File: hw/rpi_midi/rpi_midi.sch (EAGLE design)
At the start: 47 parts, among them IC1 74HC14N, X1 WBTOR1, X2 WBTOR1, X3 WBTOR1, X4 WBTOR1

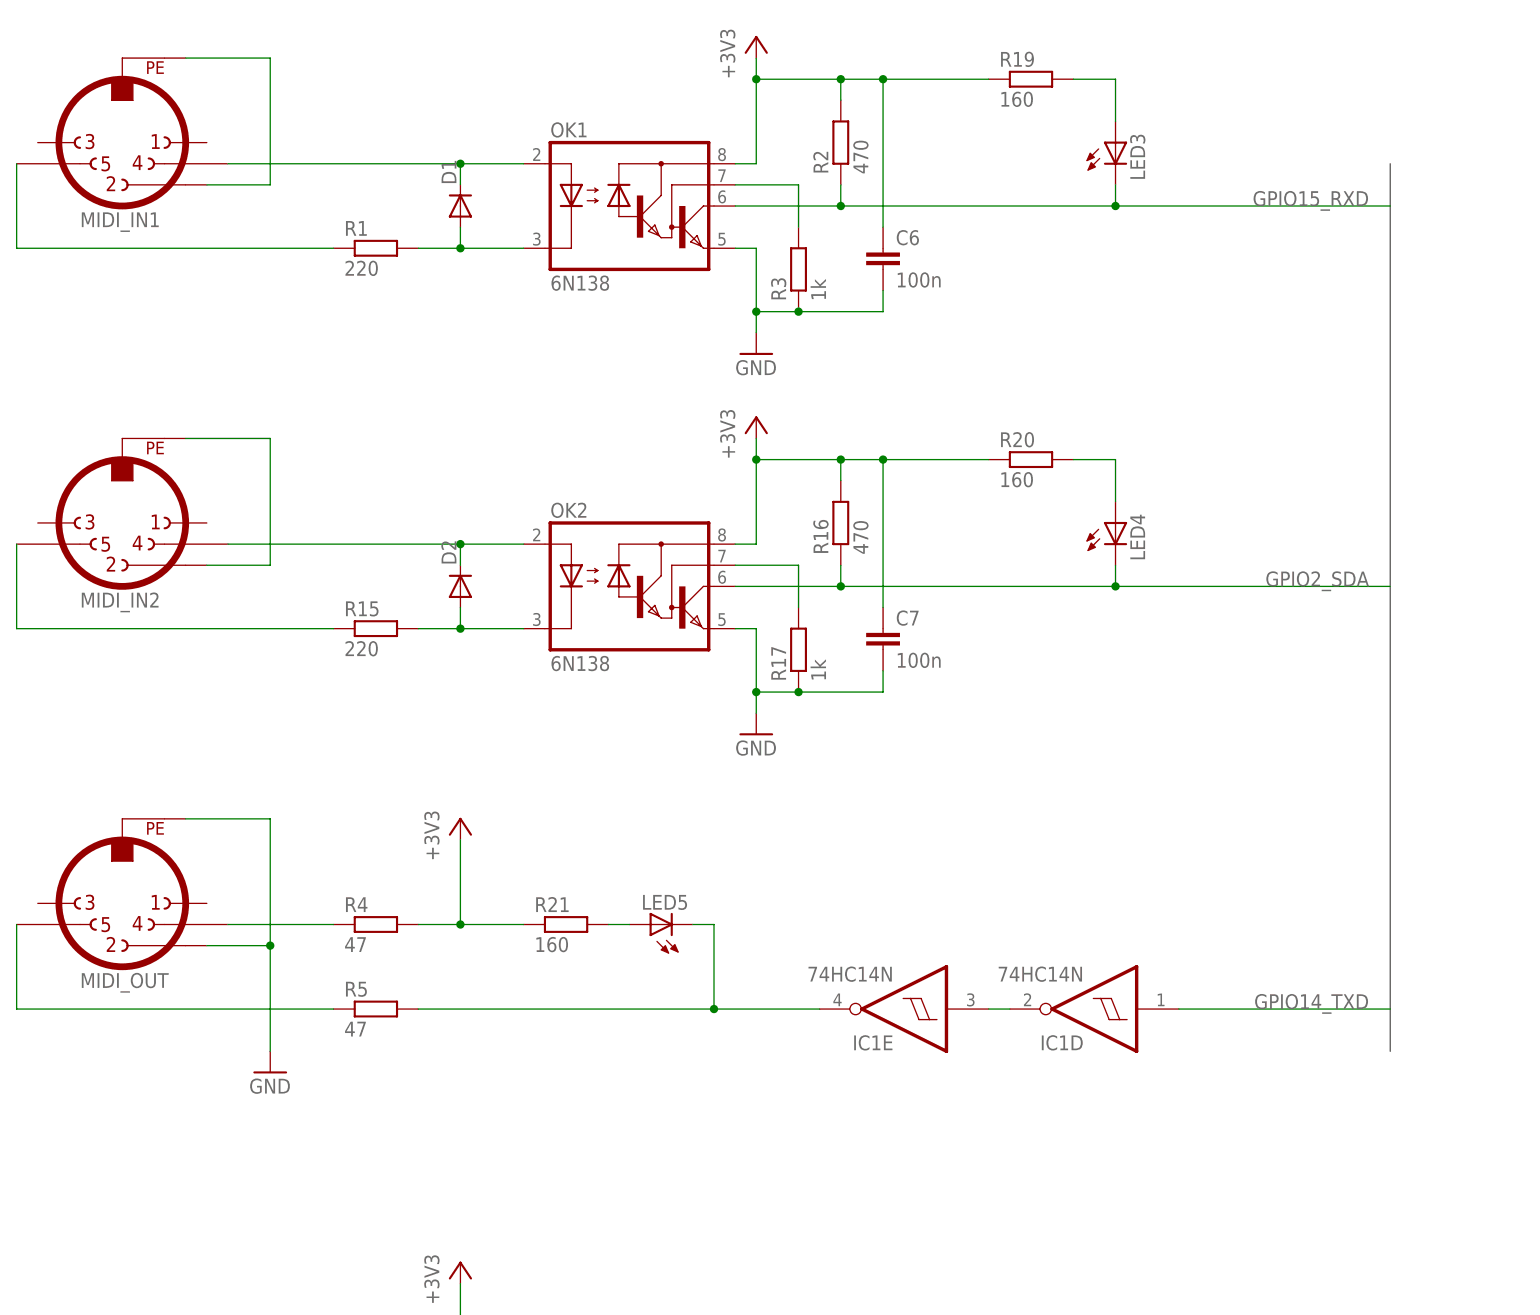
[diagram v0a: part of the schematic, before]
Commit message: The RPi MIDI extension board now features MIDI_OUT link detection capabilities
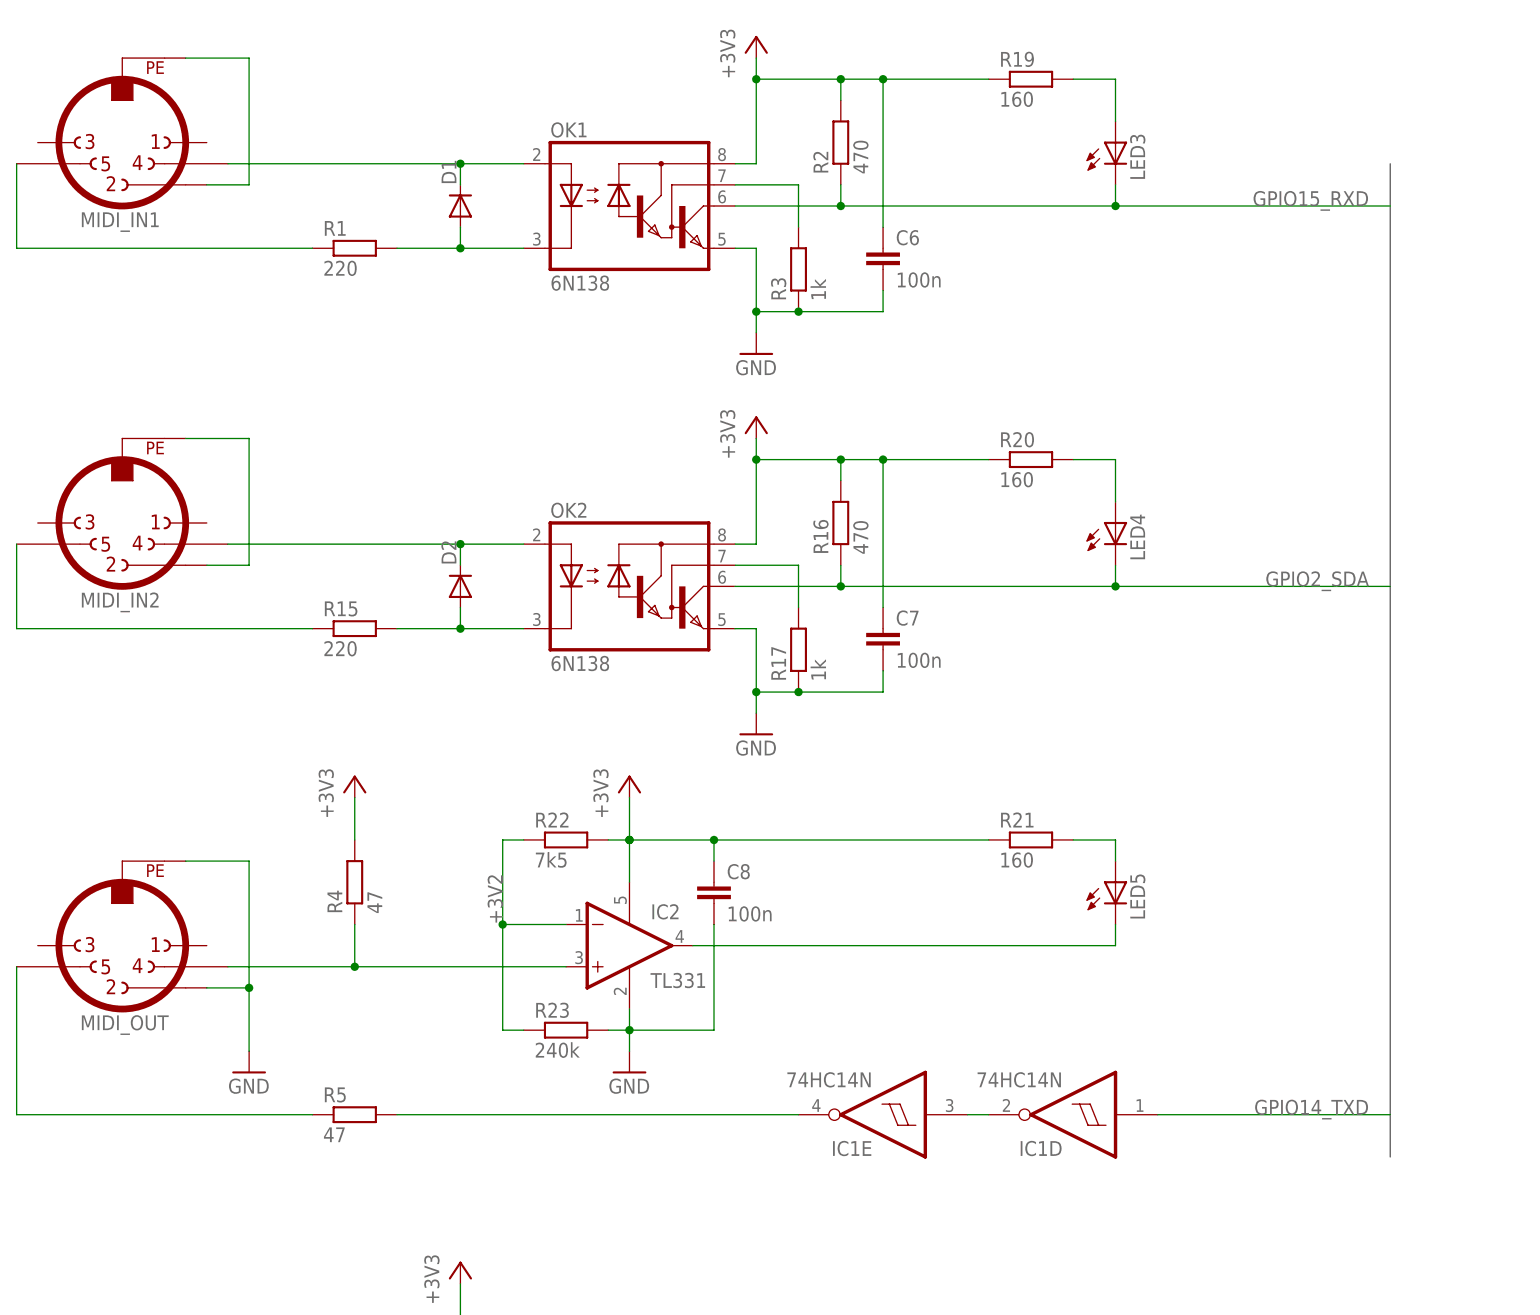
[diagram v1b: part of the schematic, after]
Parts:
- added C8: 100n, rcl:C-EU050-024X044
- added IC2: TL331, custom:TL331
- added R22: 7k5, rcl:R-EU_0207/7
- added R23: 240k, rcl:R-EU_0207/7
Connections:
- new net +3V2: IC2.-IN, R22.1, R23.1
- new net N$22: IC2.OUT, LED5.C
- net +3V3: now also C8.1, IC2.V+, R22.2
- net GND: now also C8.2, IC2.V-, R23.2
- net N$10: now also IC2.+IN
- net N$6: no longer LED5.C
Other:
- moved on the sheet: IC1D, IC1E, LED5, MIDI_OUT, R1, R15, R21, R4, R5

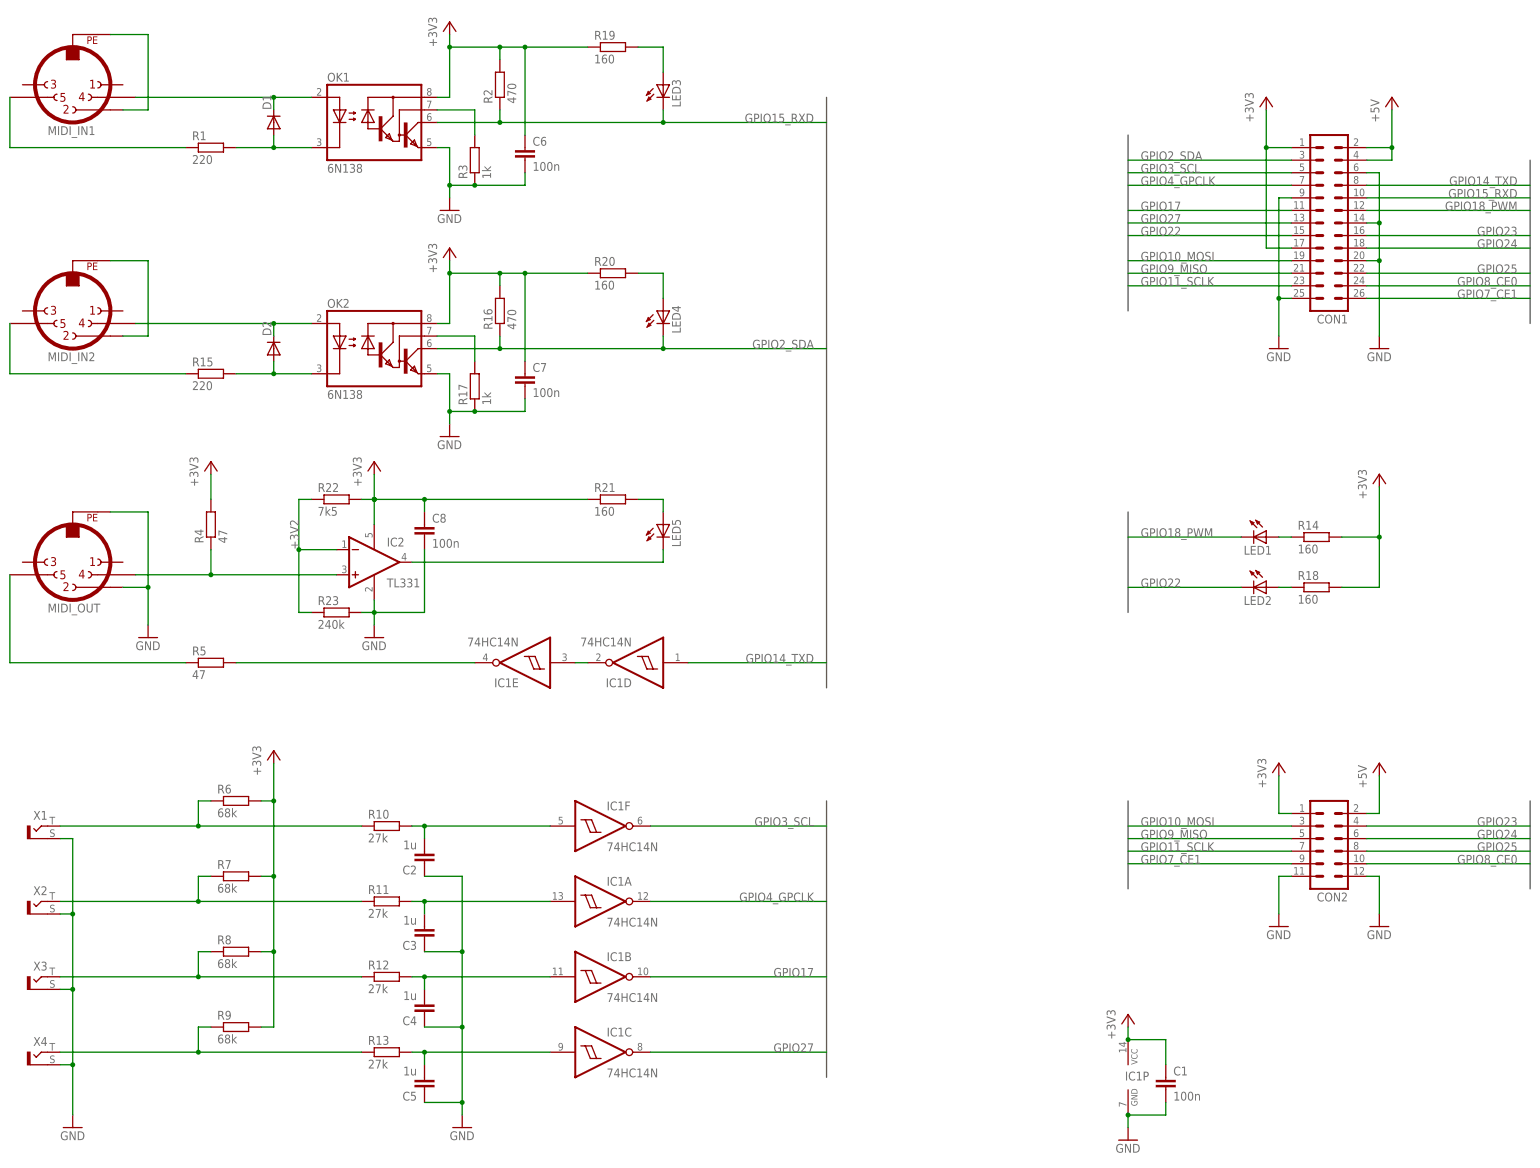
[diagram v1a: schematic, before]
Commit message: Added the most recent PCB schematic and layout files
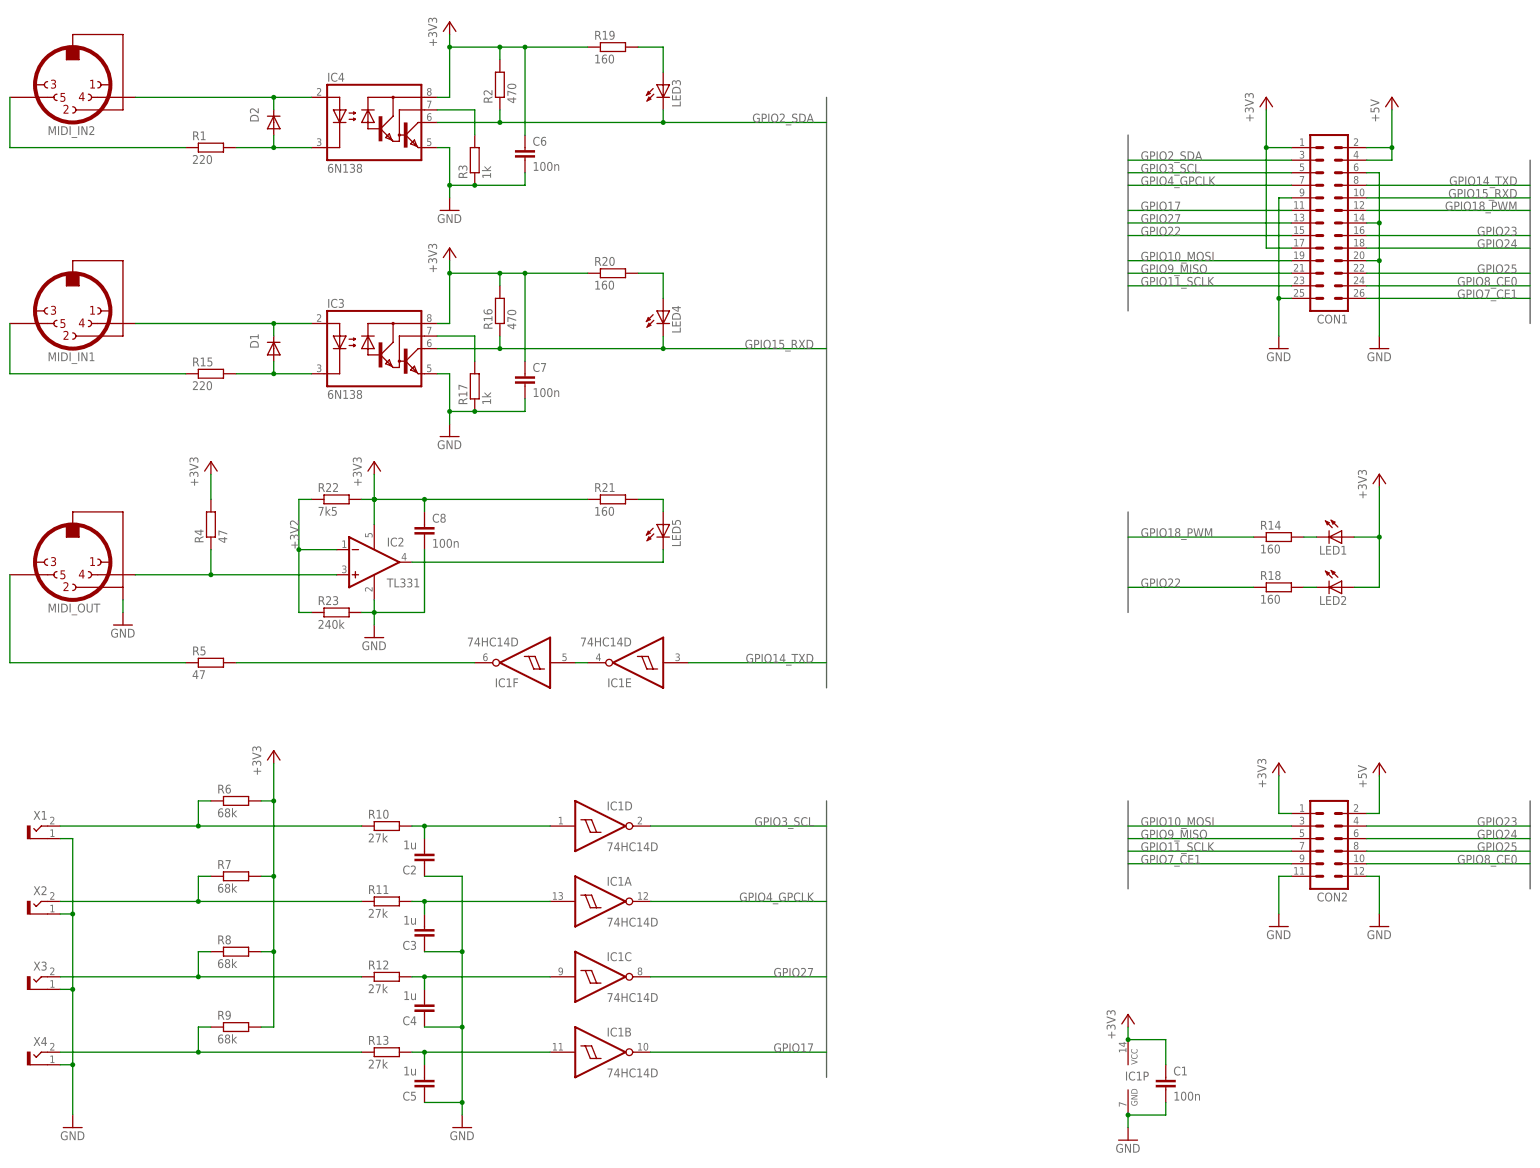
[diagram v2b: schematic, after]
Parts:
- C1, C2, C3, C4, C5, C6, C7, C8: device rcl:C-EU050-024X044 -> rcl:C-EUC0603
- D1, D2: value 1N4148DO35-7 -> 1N4148SOD-323; device diode:1N4148DO35-7 -> diode:1N4148SOD-323
- IC1: value 74HC14N -> 74HC14D; device 74xx-eu:74HC14N -> 74xx-eu:74HC14D
- LED1, LED2, LED3, LED4, LED5: device led:LED5MM -> led:LED2.54MM
- MIDI_IN1, MIDI_IN2: value MAB5SV -> MIDI_2PIN; device con-hirschmann:MAB5SV -> con-hirschmann:MIDI_2PIN
- MIDI_OUT: value MAB5SV -> MIDI_3PIN; device con-hirschmann:MAB5SV -> con-hirschmann:MIDI_3PIN
- R1, R10, R11, R12, R13, R14, R15, R16, R17, R18, R19, R2, R20, R21, R22, R23, R3, R4, R5, R6, R7, R8, R9: device rcl:R-EU_0207/7 -> rcl:R-EU_R0603
- X1, X2, X3, X4: value WBTOR1 -> WBTOR12.54MM; device con-lumberg:WBTOR1 -> con-lumberg:WBTOR12.54MM
- renumbered OK1 to IC4, OK2 to IC3
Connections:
- removed net N$21: LED2.A, R18.1
- removed net N$27: MIDI_IN2.2, MIDI_IN2.PE
- net +3V3: now also LED1.A, LED2.A; no longer R14.2, R18.2
- net GND: no longer MIDI_OUT.2
- net GPIO14_TXD: now also IC1E.I; no longer IC1D.I
- net GPIO15_RXD: now also IC3.VO, LED4.C, R16.1; no longer IC4.VO, LED3.C, R2.1
- net GPIO18_PWM: now also R14.1; no longer LED1.C
- net GPIO22: now also R18.1; no longer LED2.C
- net GPIO2_SDA: now also IC4.VO, LED3.C, R2.1; no longer IC3.VO, LED4.C, R16.1
- net GPIO3_SCL: now also IC1D.O; no longer IC1F.O
- net N$1: now also MIDI_IN2.5; no longer MIDI_IN1.5
- net N$11: now also MIDI_IN1.5; no longer MIDI_IN2.5
- net N$13: now also IC1D.I; no longer IC1F.I
- net N$18: now also IC1C.I; no longer IC1B.I
- net N$19: now also IC1B.I; no longer IC1C.I
- net N$2: now also D2.A; no longer D1.A
- net N$20: now also D1.A; no longer D2.A
- net N$26: now also D1.C, MIDI_IN1.4; no longer D2.C, MIDI_IN2.4
- net N$3: now also D2.C, MIDI_IN2.4; no longer D1.C, MIDI_IN1.4
- net N$4: now also LED1.C, R14.2; no longer MIDI_IN1.2, MIDI_IN1.PE
- net N$6: now also IC1F.O; no longer IC1E.O
- net N$7: now also LED2.C, R18.2; no longer LED1.A, R14.1
- net N$8: now also IC1E.O, IC1F.I; no longer IC1D.O, IC1E.I
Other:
- moved on the sheet: D1, D2, IC1B, IC1C, IC1D, IC1E, IC1F, LED1, LED2, R14, R18
